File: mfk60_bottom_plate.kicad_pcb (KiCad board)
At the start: 2 copper layers, 300 x 95.2 mm, 17 parts, among them T1 Tab, T2 Tab, T3 Tab, T4 Tab, T5 Tab, T6 Tab, T7 Tab

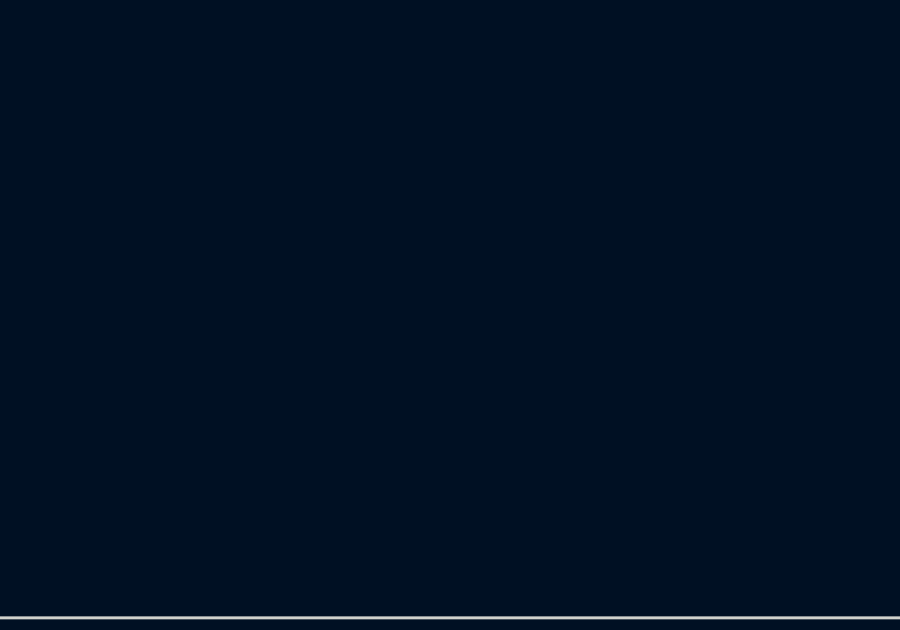
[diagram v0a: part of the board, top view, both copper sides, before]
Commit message: Adjust JLC text position and add it to script.
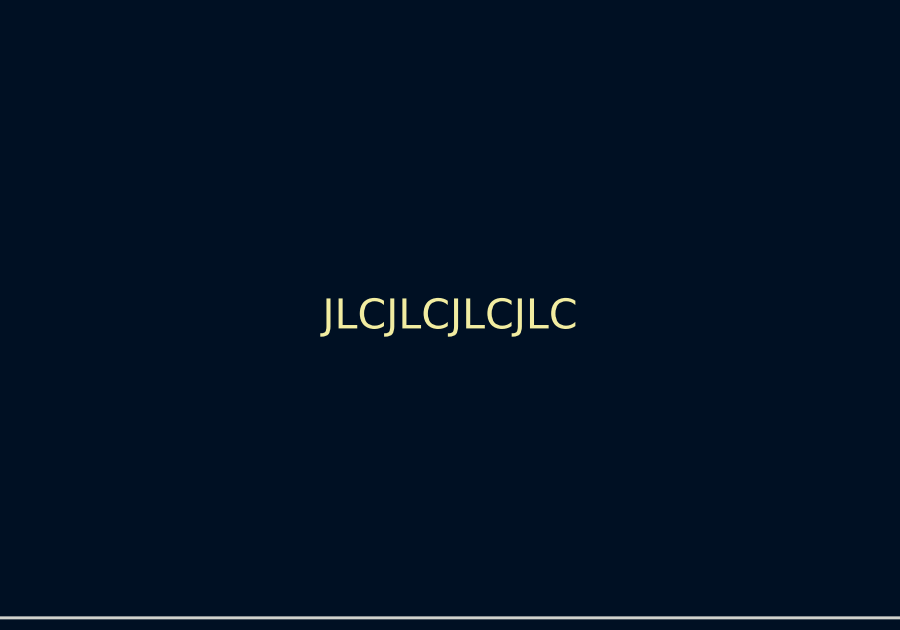
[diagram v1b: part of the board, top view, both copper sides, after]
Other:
- board text added: "JLCJLCJLCJLC"
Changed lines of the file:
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@@
   (gr_arc (start 137.3 25) (mid 138.714214 25.585786) (end 139.3 27)
     (stroke (width 0.1) (type default)) (layer "Edge.Cuts"))
+  (gr_text "JLCJLCJLCJLC" (at 297.653125 110.725) (layer "F.SilkS")
+    (effects (font (size 1 1) (thickness 0.15)) (justify bottom))
+  )
 )
